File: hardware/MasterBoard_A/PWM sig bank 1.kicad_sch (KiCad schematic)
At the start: 45 parts, among them Q16 MMBT5550L, Q17 MMBT5550L, Q4 MMBT5550L, Q6 MMBT5550L, Q7 MMBT5550L, Q8 MMBT5550L, U15 TLP155E, U16 TLP155E, U17 TLP155E, U20 IPD70R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

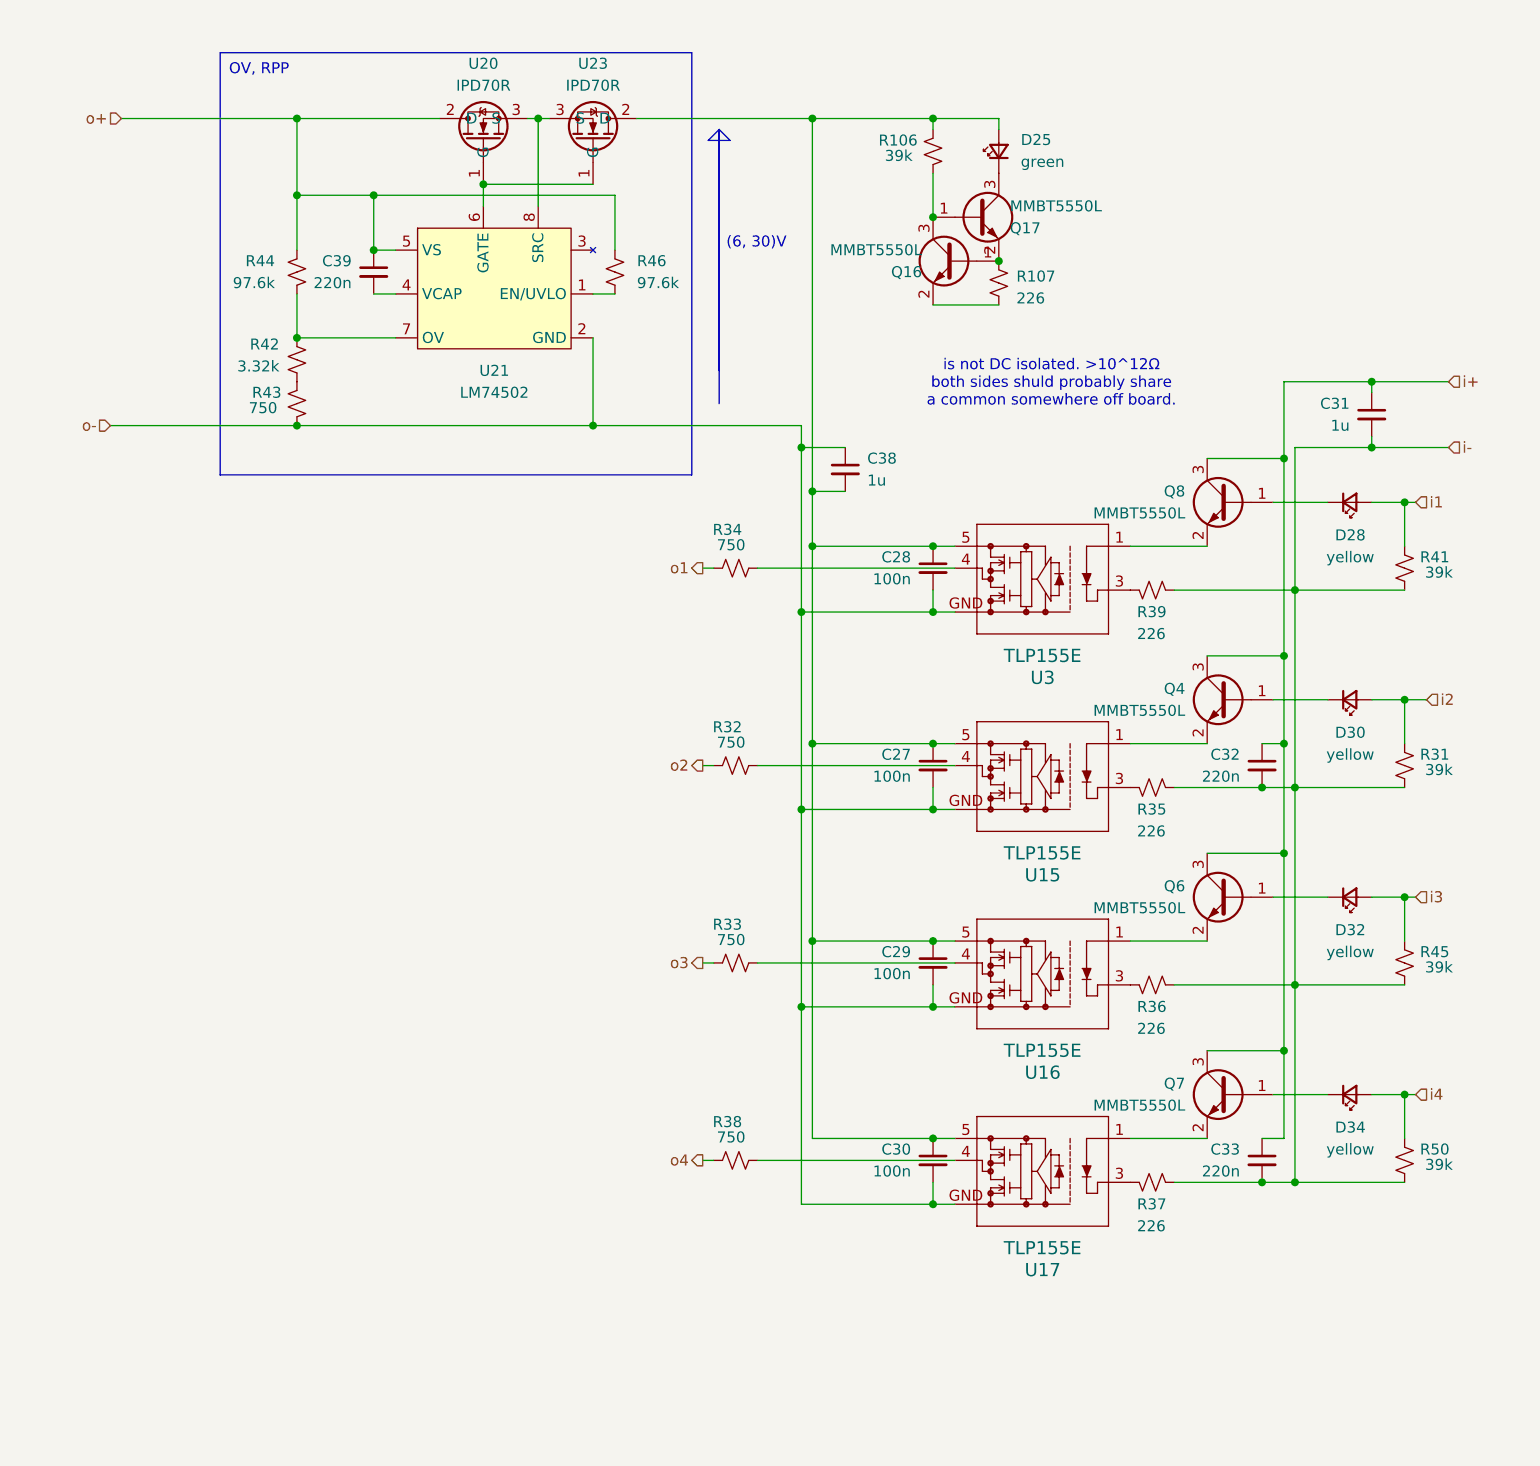
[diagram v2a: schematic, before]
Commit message: better-ified power stuff. new costing program
handy new costing program for kicad. just c&p symbols directly from kicad into it and itll dump out the BOM cost of what ever you gave it
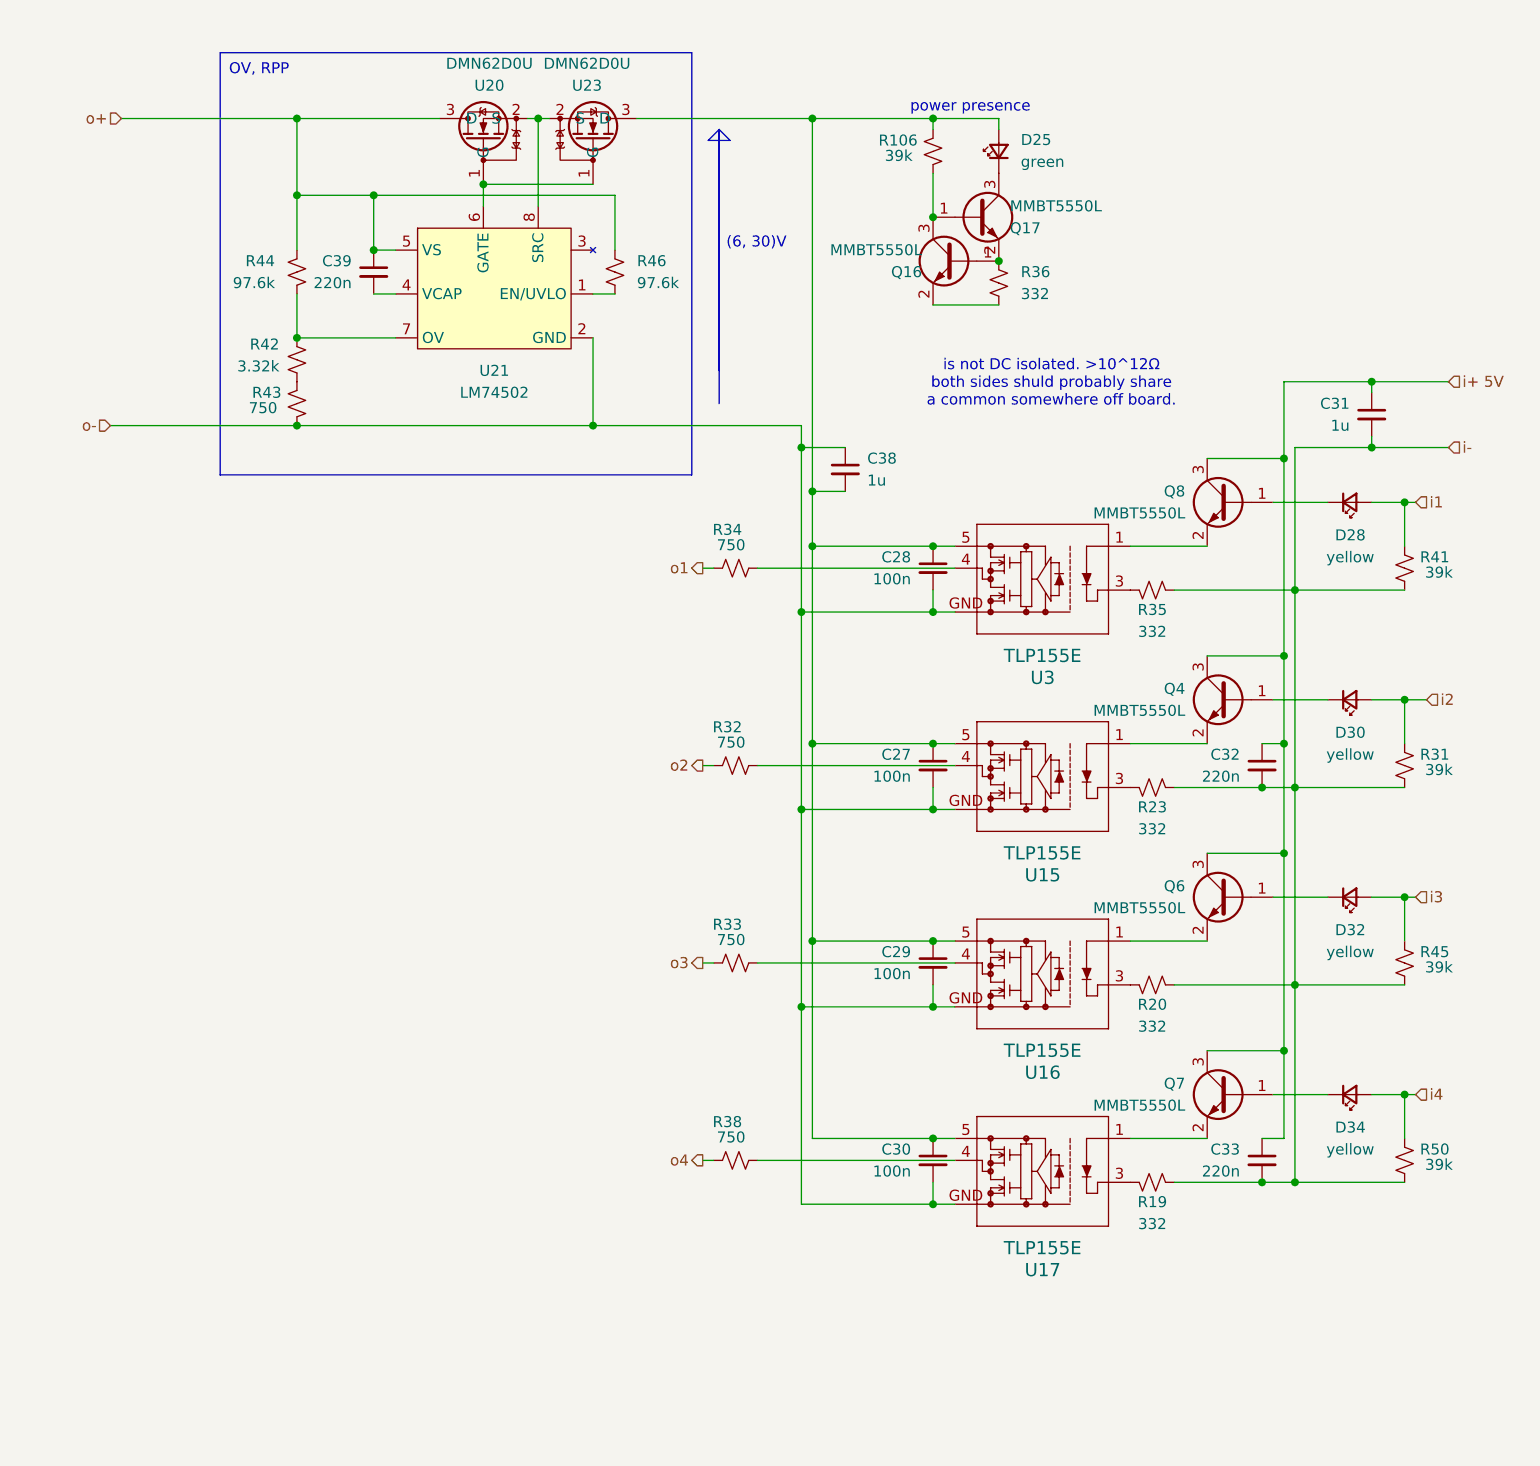
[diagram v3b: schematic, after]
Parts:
- removed R107, R37, R39: 226, Resistor_SMD:R_0805_2012Metric_Pad1.20x1.40mm_HandSolder, symbol Device:R_Small_US
- removed U20, U23: IPD70R, Package_TO_SOT_SMD:TO-252-2, symbol zzLocalLibrary:IPD70R
- added R19, R20, R23: 332, Resistor_SMD:R_1206_3216Metric_Pad1.30x1.75mm_HandSolder, symbol Device:R_Small_US
- added U20, U23: DMN62D0U, Package_TO_SOT_SMD:SOT-23_Handsoldering, symbol zzLocalLibrary:DMN62D0U
- R35, R36: value 226 -> 332; footprint Resistor_SMD:R_0805_2012Metric_Pad1.20x1.40mm_HandSolder -> Resistor_SMD:R_1206_3216Metric_Pad1.30x1.75mm_HandSolder; mouser https://www.mouser.com/ProductDetail/KOA-Speer/RK73H2BTTD22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 -> https://www.mouser.com/ProductDetail/YAGEO/AC1206FR-07332RL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; specs 226Ohm, 250mW, 1%, 200V, -55C, +155C -> 332 ohm, 250mW, 200V, 1%, 100ppm, -55C, +155C; unit x10 0.023 -> 0.016
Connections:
- net i-: now also R19.2, R20.2, R23.2; no longer R36.2
- net o+: now also U20.3 (D)
- net at U15.3: now also R23.1; no longer R35.1
- net at C27.1, C28.1, C29.1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: now also U23.3 (D)
- net at U16.3: now also R20.1; no longer R36.1
- net at U17.3: now also R19.1
- net at Q16.1 (B), Q17.2 (E): now also R36.1
- net at Q16.2 (E): now also R36.2
- net at U21.6 (GATE): now also U20.1 (G), U23.1 (G)
- net at U21.8 (SRC): now also U20.2 (S), U23.2 (S)
- net at U3.3: now also R35.1
- net i+ renamed i+ 5V
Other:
- note added: "power presence"

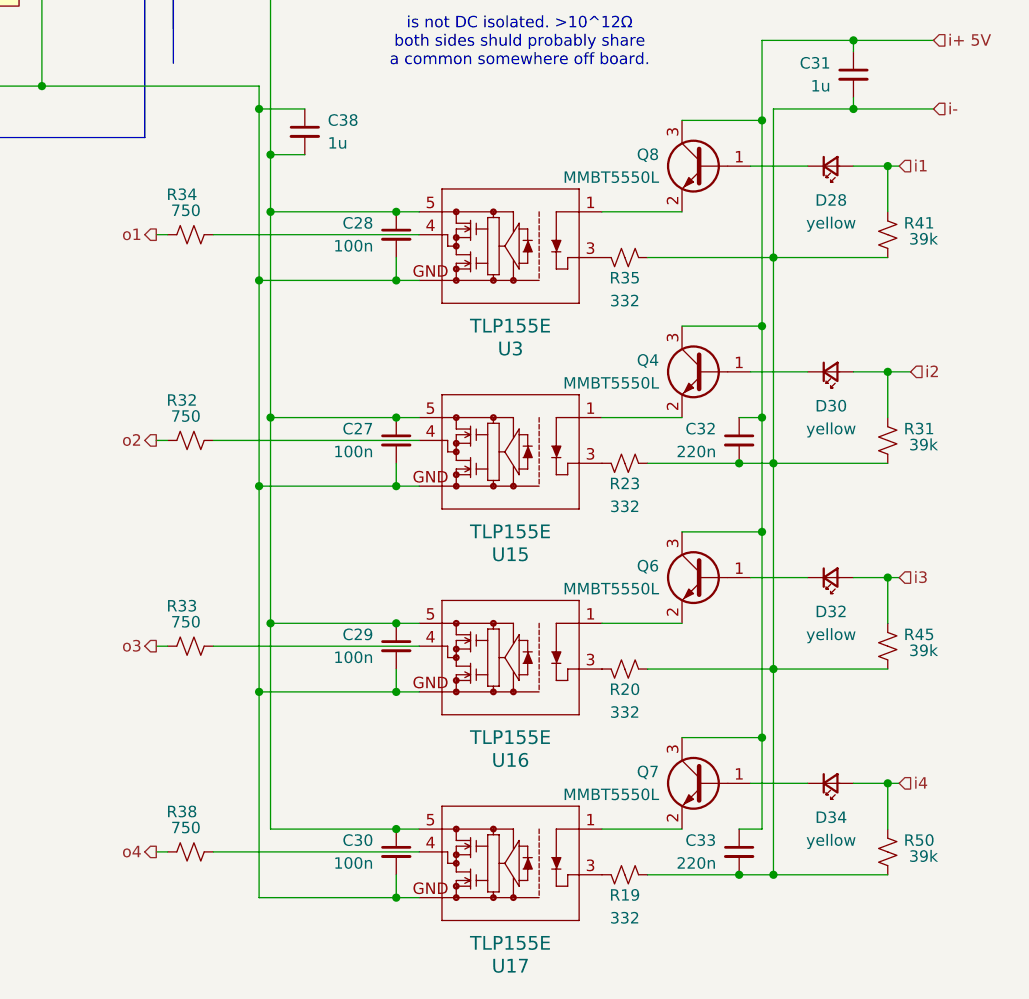
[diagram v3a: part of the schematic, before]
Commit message: near final
missing direct MCU connections, pin map excel sheet needs piddled with. schematic needs reviewed
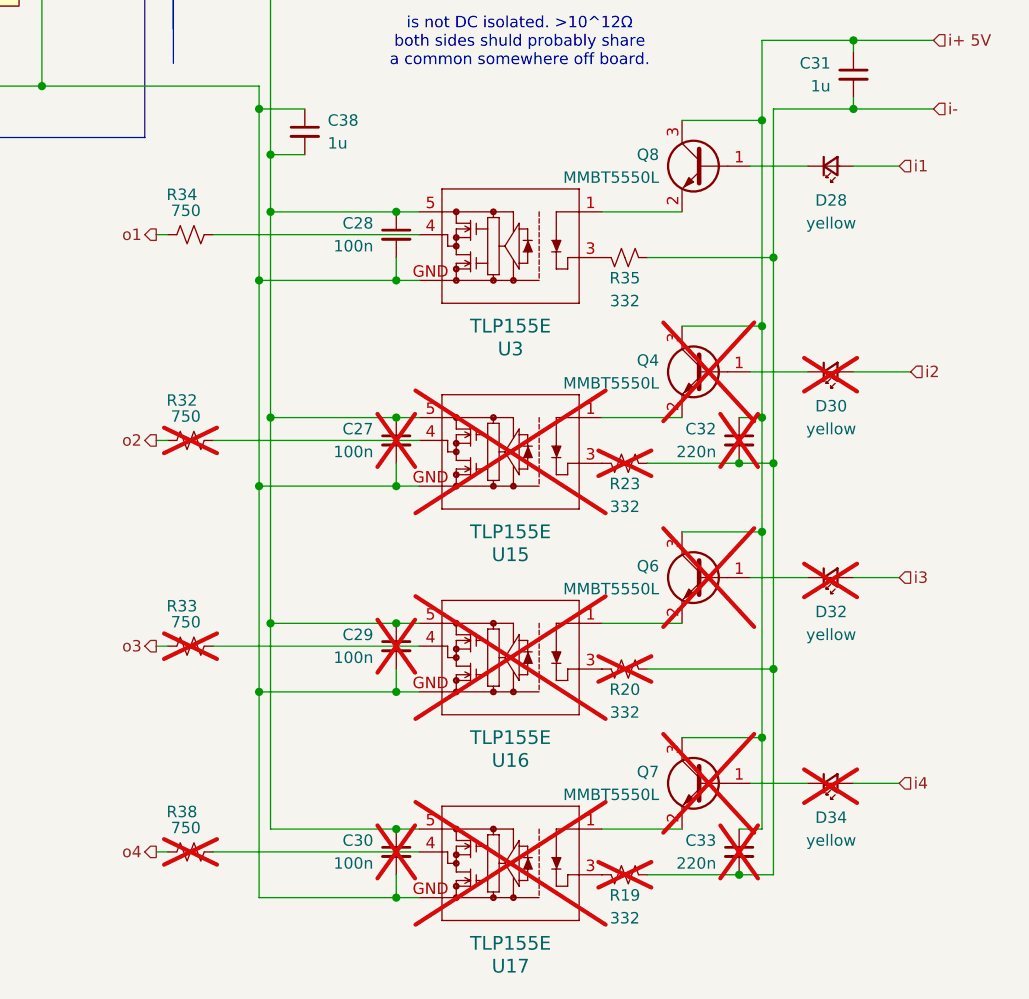
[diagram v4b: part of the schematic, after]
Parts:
- removed R31, R41, R45, R50: 39k, Resistor_SMD:R_0805_2012Metric_Pad1.20x1.40mm_HandSolder, symbol Device:R_Small_US
- C27, C29, C30, C32, C33, D30, D32, D34, Q4, Q6, Q7, R19, R20, R23, R32, R33, R38, U15, U16, U17: now not fitted; now left out of the parts list

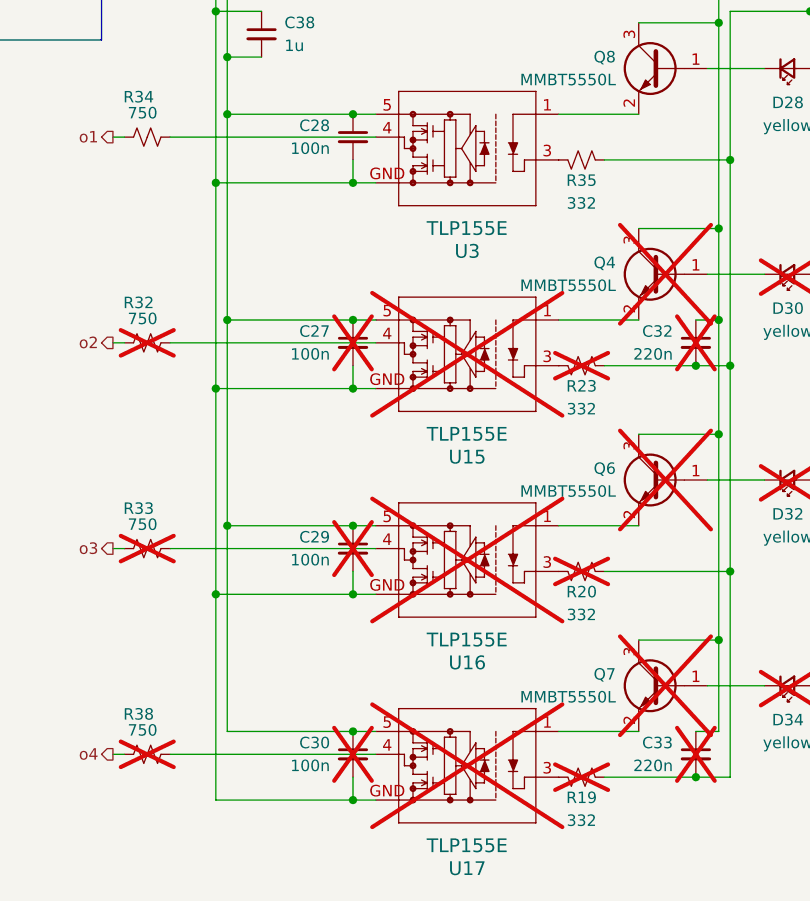
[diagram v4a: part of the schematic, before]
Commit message: one must have hope
eyeballed the ethernet transmission lines, i think it'll work. absolute pain without using footprints smaller than 0805 but it think itll be fine. also shuffled together the PWM sig bank
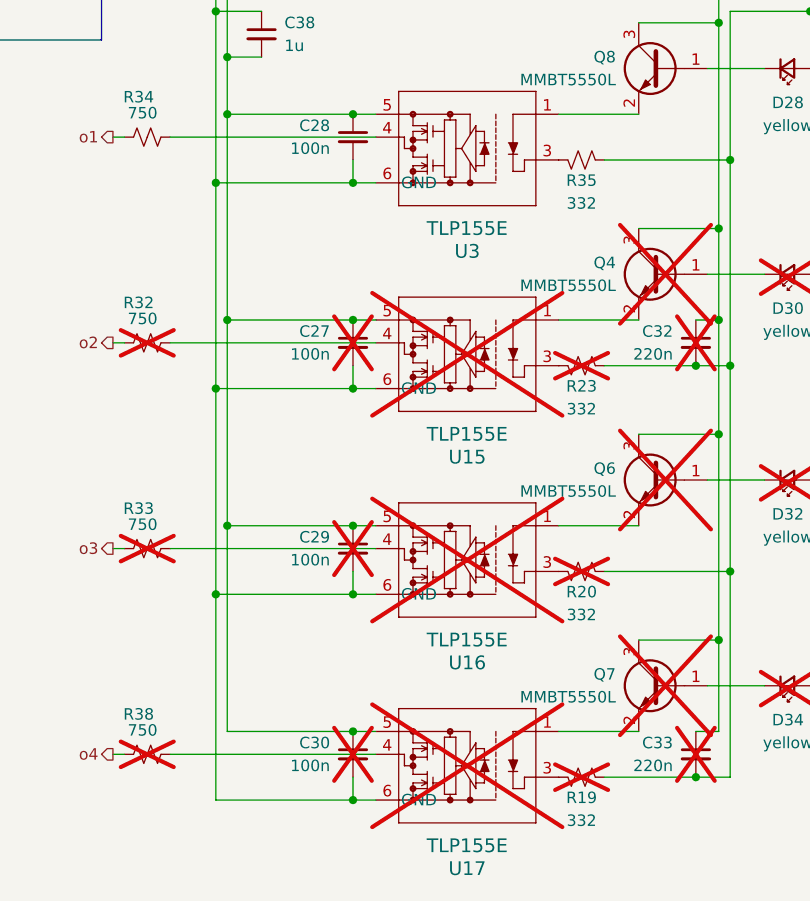
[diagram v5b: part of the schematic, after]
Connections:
- net o-: now also U15.6 (GND), U16.6 (GND), U17.6 (GND), U3.6 (GND); no longer U15.GND, U16.GND, U17.GND, U3.GND

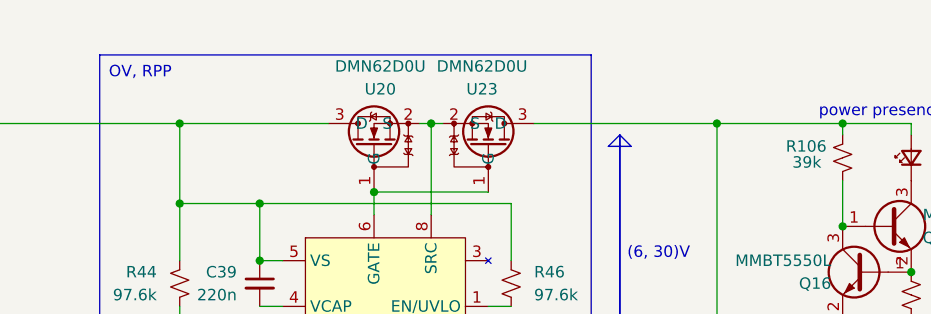
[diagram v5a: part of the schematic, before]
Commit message: partial layout of psu
pdn about to look like a mine field
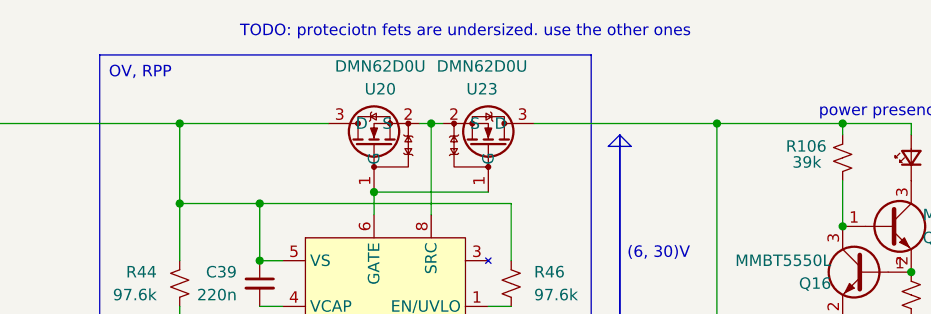
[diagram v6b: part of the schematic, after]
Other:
- note added: "TODO: proteciotn fets are undersized. use the other ones"
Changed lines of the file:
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@@
+		)
+	)
+	(text "TODO: proteciotn fets are undersized. use the other ones"
+		(exclude_from_sim no)
+		(at 77.47 26.67 0)
+		(effects
+			(font
+				(size 1.27 1.27)
+			)
 		)
 	)

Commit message: up to date meta sheet and made release files
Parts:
- C28: mouser https://www.mouser.com/ProductDetail/Walsin/1206B104K251CT?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 -> https://www.mouser.com/ProductDetail/Walsin/1206B104K201CT?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; specs 100nF, 250VDC, X7R, 10%, -55C, +125C -> 100nF, 200VDC, X7R, 10%, -55C, +125C; unit x1 (none) -> 0.11; unit x10 0.042 -> 0.045
- C39: unit x1 (none) -> 0.054
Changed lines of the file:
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@@
 			)
 		)
-		(property "mouser" "https://www.mouser.com/ProductDetail/Walsin/1206B104K251CT?qs=fIkAfuXiAQKkmX5niKUTKw%3D%3D"
+		(property "mouser" "https://www.mouser.com/ProductDetail/Walsin/1206B104K201CT?qs=fIkAfuXiAQKvqIFf8la7zg%3D%3D"
 			(at 119.38 88.9 0)
 			(effects
@@
 			)
 		)
-		(property "specs" "100nF, 250VDC, X7R, 10%, -55C, +125C"
+		(property "specs" "100nF, 200VDC, X7R, 10%, -55C, +125C"
 			(at 119.38 88.9 0)
 			(effects
@@
 			)
 		)
-		(property "unit x10" "0.042"
+		(property "unit x10" "0.045"
 			(at 119.38 88.9 0)
 			(effects
@@
 		)
 		(property "note" ""
+			(at 119.38 88.9 0)
+			(effects
+				(font
+					(size 1.27 1.27)
+				)
+				(hide yes)
+			)
+		)
+		(property "unit x1" "0.11"
 			(at 119.38 88.9 0)
 			(effects
@@
 			(at 54.61 54.61 0)
 			(effects
+				(font
+					(size 1.27 1.27)
+				)
+				(hide yes)
+			)
+		)
+		(property "unit x1" "0.054"
+			(at 54.61 54.61 0)
+			(effects
